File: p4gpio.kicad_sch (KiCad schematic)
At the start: 4 parts, among them J1 C2760486, J2 C2760486

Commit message: Start work on layout
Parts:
- added J10, J9: Conn_01x04_Socket, Connector_PinSocket_2.54mm:PinSocket_1x04_P2.54mm_Vertical, symbol Connector:Conn_01x04_Socket
- added J3, J4, J5, J6, J7, J8: Conn_01x08_Pin, Connector_PinHeader_2.54mm:PinHeader_1x08_P2.54mm_Vertical, symbol Connector:Conn_01x08_Pin
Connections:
- net GND: now also J10.3 (Pin_3), J9.3 (Pin_3)
- net Minimal P4 V3/BOOT renamed BOOT
- net BOOT: now also J10.2 (Pin_2), J9.2 (Pin_2)
- net Minimal P4 V3/CHIP_PU renamed RESET
- net RESET: now also J10.4 (Pin_4), J9.4 (Pin_4)
- new net +3.3V: J10.1 (Pin_1), J9.1 (Pin_1)
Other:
- moved on the sheet: J1, J2

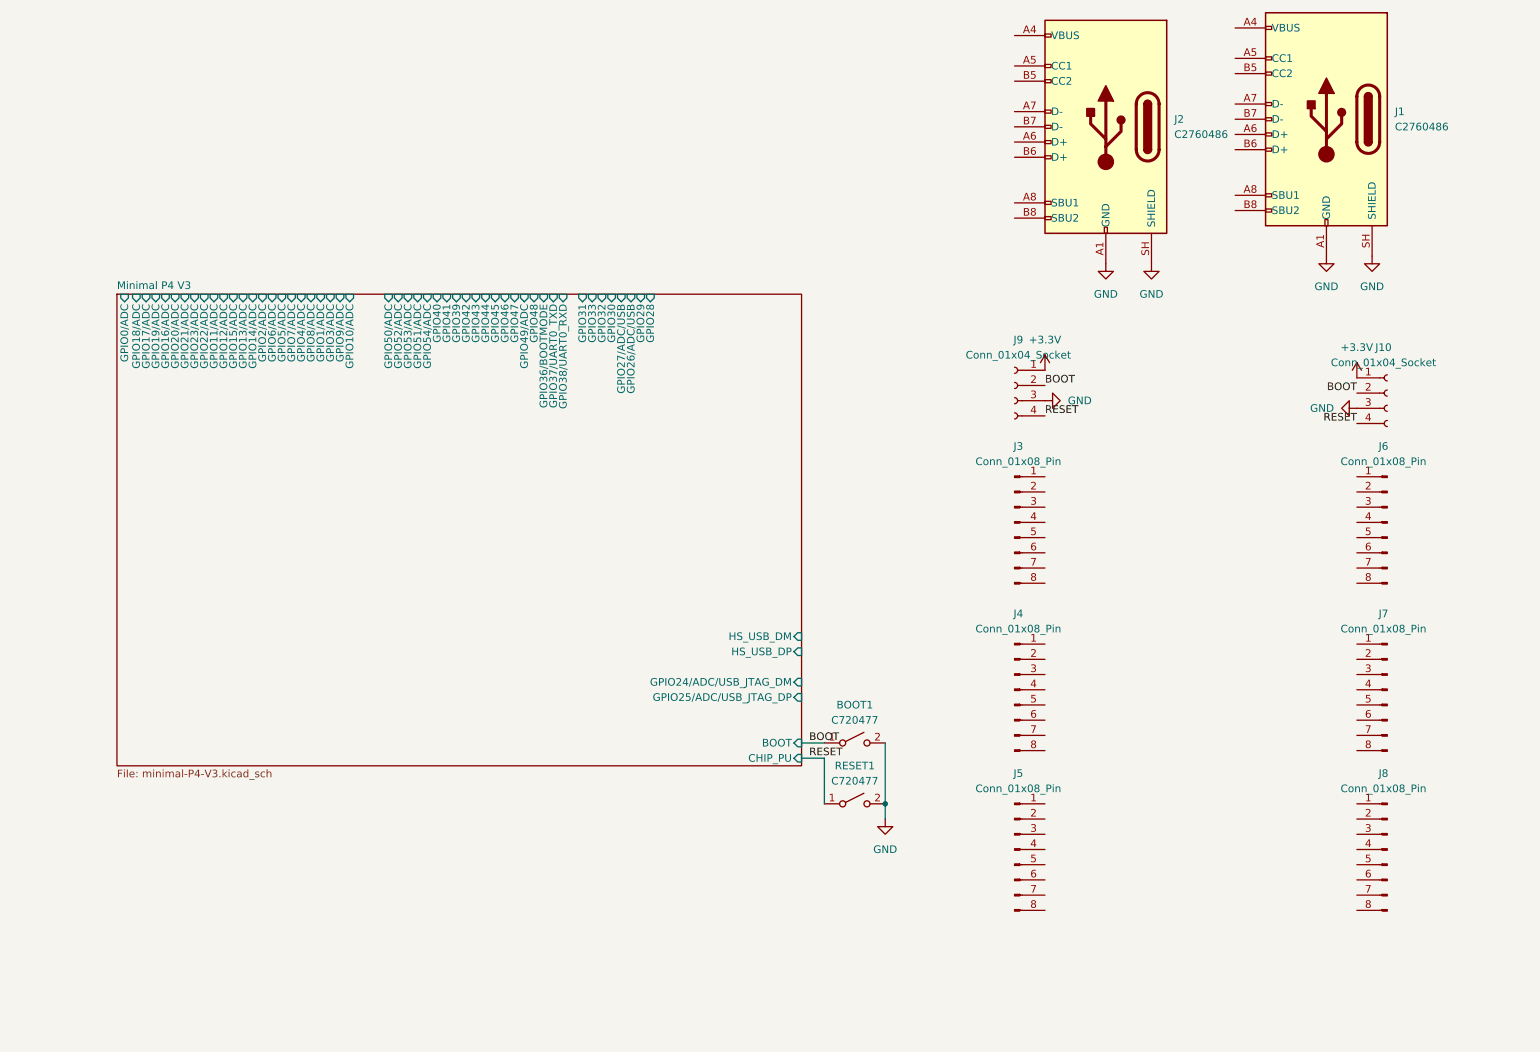
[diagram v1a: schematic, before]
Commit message: Schematic done except for GPIO
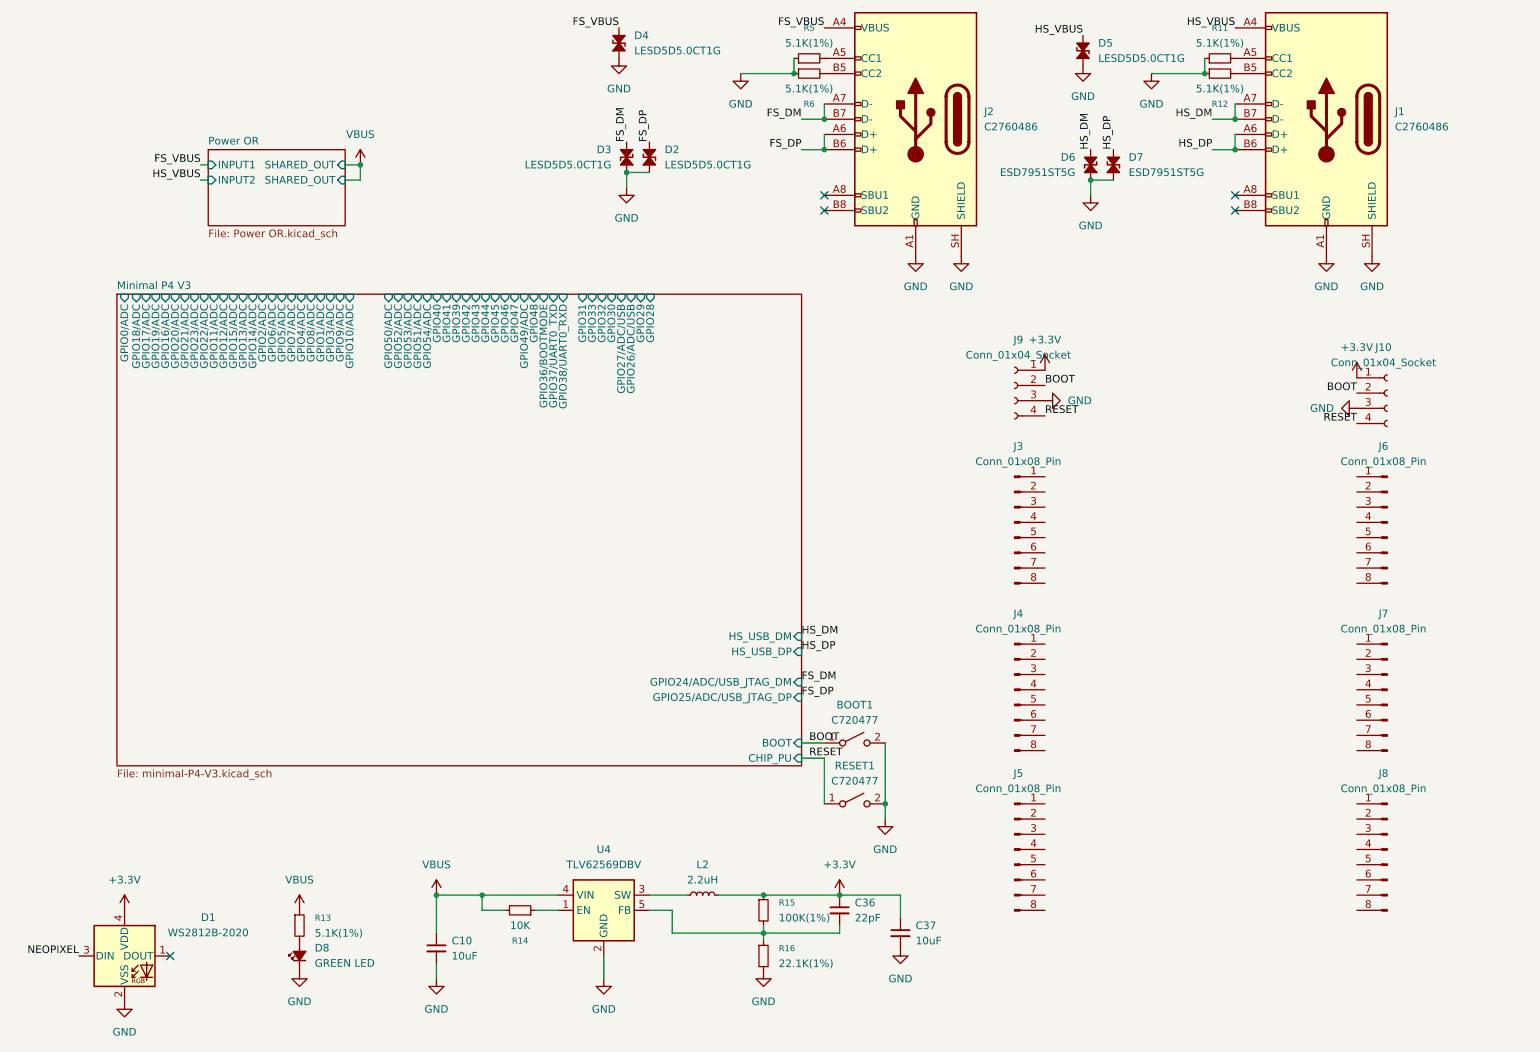
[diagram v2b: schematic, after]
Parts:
- added C10, C37: 10uF, Capacitor_SMD:C_0603_1608Metric, symbol Device:C_Small
- added C36: 22pF, Capacitor_SMD:C_0402_1005Metric, symbol Device:C_Small
- added D1: WS2812B-2020, LED_SMD:LED_WS2812B-2020_PLCC4_2.0x2.0mm, symbol LED:WS2812B-2020
- added D2, D3, D4, D5: LESD5D5.0CT1G, Diode_SMD:D_SOD-523, symbol Device:D_TVS_Small_Filled
- added D6, D7: ESD7951ST5G, Diode_SMD:D_SOD-882, symbol Device:D_TVS_Small_Filled
- added D8: GREEN LED, Diode_SMD:D_0805_2012Metric, symbol Device:LED_Small_Filled
- added L2: 2.2uH, Inductor_SMD:L_1008_2520Metric, symbol Device:L_Small
- added R11, R12, R13, R5, R6: 5.1K(1%), Resistor_SMD:R_0402_1005Metric, symbol Device:R_Small
- added R14: 10K, Resistor_SMD:R_0402_1005Metric, symbol Device:R_Small
- added R15: 100K(1%), Resistor_SMD:R_0402_1005Metric, symbol Device:R_Small
- added R16: 22.1K(1%), Resistor_SMD:R_0402_1005Metric, symbol Device:R_Small
- added U4: TLV62569DBV, Package_TO_SOT_SMD:SOT-23-5, symbol Regulator_Switching:TLV62569DBV
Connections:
- net +3.3V: now also C36.1, C37.1, D1.4 (VDD), L2.2, R15.1
- net GND: now also C10.2, C37.2, D1.2 (VSS), D2.1 (A1), D3.1 (A1), D4.1 (A1), D5.1 (A1), D6.1 (A1), D7.1 (A1), D8.1 (K), R11.1, R12.1, R16.2, R5.1, R6.1, U4.2 (GND)
- net HS_VBUS: now reaches J1.A4 (VBUS), J1.A9 (VBUS), J1.B4 (VBUS), J1.B9 (VBUS)
- net HS_VBUS: now also D5.2 (A2)
- net at J1.A5 (CC1): now also R11.2
- net HS_DP: now reaches J1.A6 (D+)
- net HS_DP: now also J1.B6 (D+), D7.2 (A2)
- net HS_DM: now reaches J1.A7 (D-)
- net HS_DM: now also J1.B7 (D-), D6.2 (A2)
- net at J1.B5 (CC2): now also R12.2
- net FS_VBUS: now reaches J2.A4 (VBUS), J2.A9 (VBUS), J2.B4 (VBUS), J2.B9 (VBUS)
- net FS_VBUS: now also D4.2 (A2)
- net at J2.A5 (CC1): now also R5.2
- net FS_DP: now reaches J2.A6 (D+)
- net FS_DP: now also J2.B6 (D+), D2.2 (A2)
- net FS_DM: now reaches J2.A7 (D-)
- net FS_DM: now also J2.B7 (D-), D3.2 (A2)
- net at J2.B5 (CC2): now also R6.2
- new net: R14.1, U4.1 (EN)
- new net: L2.1, U4.3 (SW)
- new net: C36.2, R15.2, R16.1, U4.5 (FB)
- new net: D8.2 (A), R13.2
- new net NEOPIXEL: D1.3 (DIN)
- new net VBUS: C10.1, R13.1, R14.2, U4.4 (VIN)
- no-connect marks 0 -> 5
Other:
- added sheet Power OR (Power OR.kicad_sch)
- moved on the sheet: J2

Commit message: Setup design rules. Start to match up pins
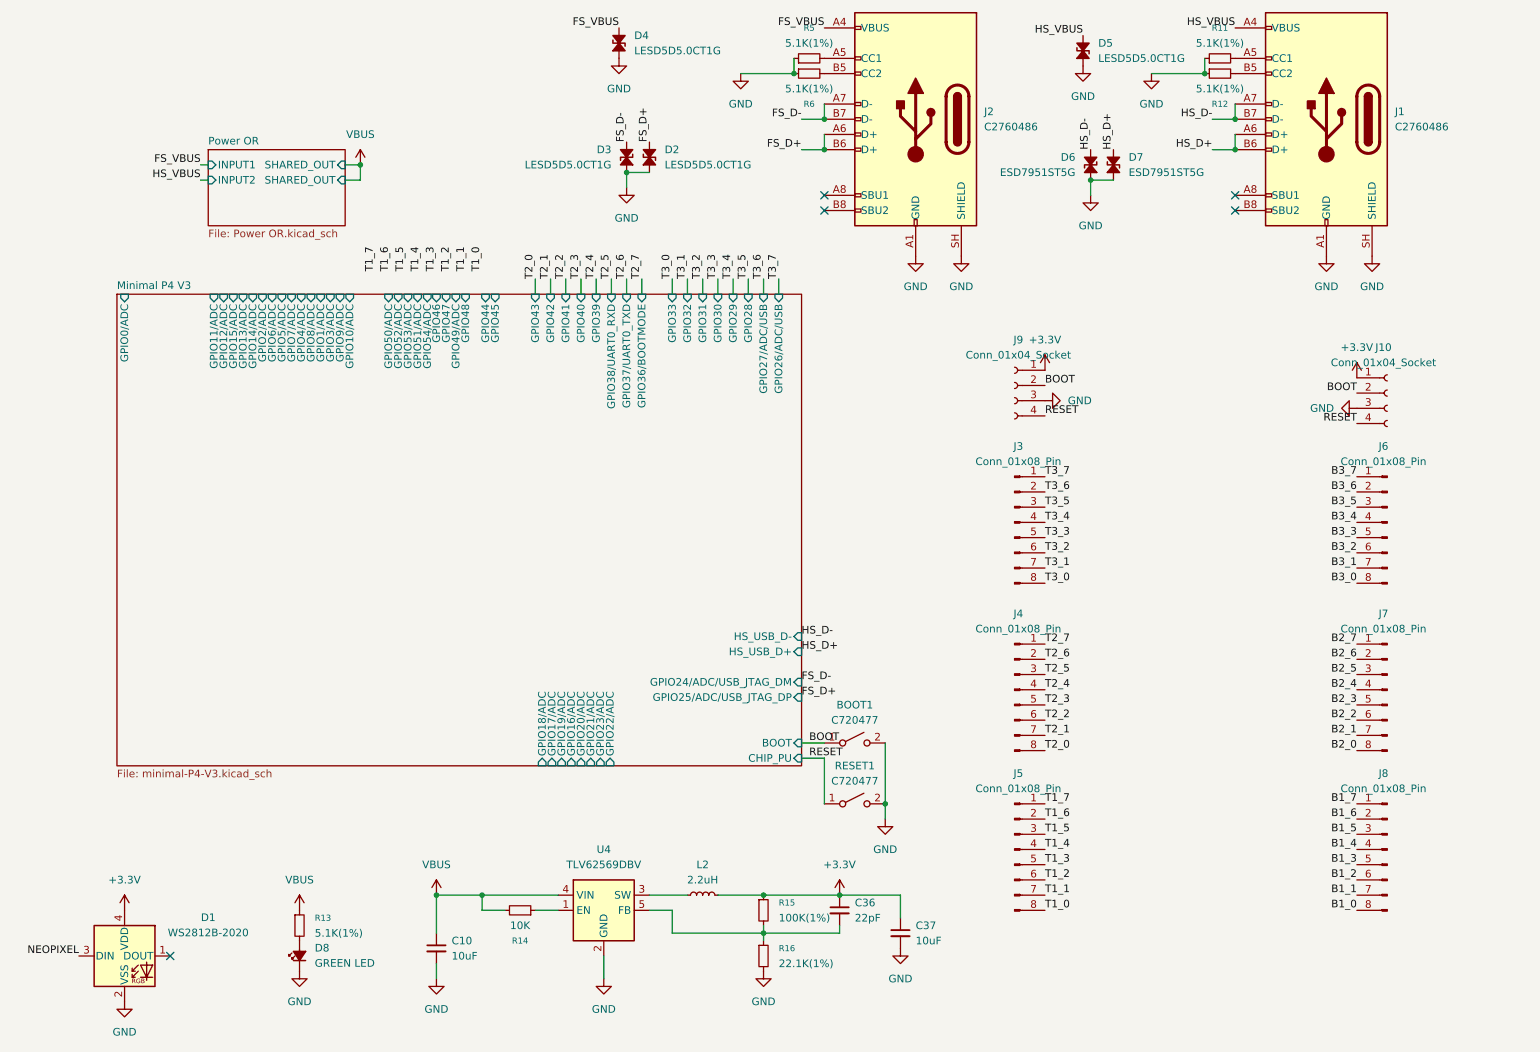
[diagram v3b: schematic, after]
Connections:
- net B3_7: now reaches J6.1 (Pin_1)
- net B3_6: now reaches J6.2 (Pin_2)
- net B3_5: now reaches J6.3 (Pin_3)
- net B3_4: now reaches J6.4 (Pin_4)
- net B3_3: now reaches J6.5 (Pin_5)
- net B3_2: now reaches J6.6 (Pin_6)
- net B3_1: now reaches J6.7 (Pin_7)
- net B3_0: now reaches J6.8 (Pin_8)
- net T2_7: now reaches J4.1 (Pin_1)
- net T2_6: now reaches J4.2 (Pin_2)
- net T2_5: now reaches J4.3 (Pin_3)
- net T2_4: now reaches J4.4 (Pin_4)
- net T2_3: now reaches J4.5 (Pin_5)
- net T2_2: now reaches J4.6 (Pin_6)
- net T2_1: now reaches J4.7 (Pin_7)
- net T2_0: now reaches J4.8 (Pin_8)
- net T3_7: now reaches J3.1 (Pin_1)
- net T3_6: now reaches J3.2 (Pin_2)
- net T3_5: now reaches J3.3 (Pin_3)
- net T3_4: now reaches J3.4 (Pin_4)
- net T3_3: now reaches J3.5 (Pin_5)
- net T3_2: now reaches J3.6 (Pin_6)
- net T3_1: now reaches J3.7 (Pin_7)
- net T3_0: now reaches J3.8 (Pin_8)
- net B2_7: now reaches J7.1 (Pin_1)
- net B2_6: now reaches J7.2 (Pin_2)
- net B2_5: now reaches J7.3 (Pin_3)
- net B2_4: now reaches J7.4 (Pin_4)
- net B2_3: now reaches J7.5 (Pin_5)
- net B2_2: now reaches J7.6 (Pin_6)
- net B2_1: now reaches J7.7 (Pin_7)
- net B2_0: now reaches J7.8 (Pin_8)
- net T1_7: now reaches J5.1 (Pin_1)
- net T1_6: now reaches J5.2 (Pin_2)
- net T1_5: now reaches J5.3 (Pin_3)
- net T1_4: now reaches J5.4 (Pin_4)
- net T1_3: now reaches J5.5 (Pin_5)
- net T1_2: now reaches J5.6 (Pin_6)
- net T1_1: now reaches J5.7 (Pin_7)
- net T1_0: now reaches J5.8 (Pin_8)
- net B1_7: now reaches J8.1 (Pin_1)
- net B1_6: now reaches J8.2 (Pin_2)
- net B1_5: now reaches J8.3 (Pin_3)
- net B1_4: now reaches J8.4 (Pin_4)
- net B1_3: now reaches J8.5 (Pin_5)
- net B1_2: now reaches J8.6 (Pin_6)
- net B1_1: now reaches J8.7 (Pin_7)
- net B1_0: now reaches J8.8 (Pin_8)
- net FS_DM renamed FS_D-
- net FS_DP renamed FS_D+
- net HS_DM renamed HS_D-
- net HS_DP renamed HS_D+
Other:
- sheet Minimal P4 V3 ports: added HS_USB_D+, HS_USB_D-; removed HS_USB_DM, HS_USB_DP

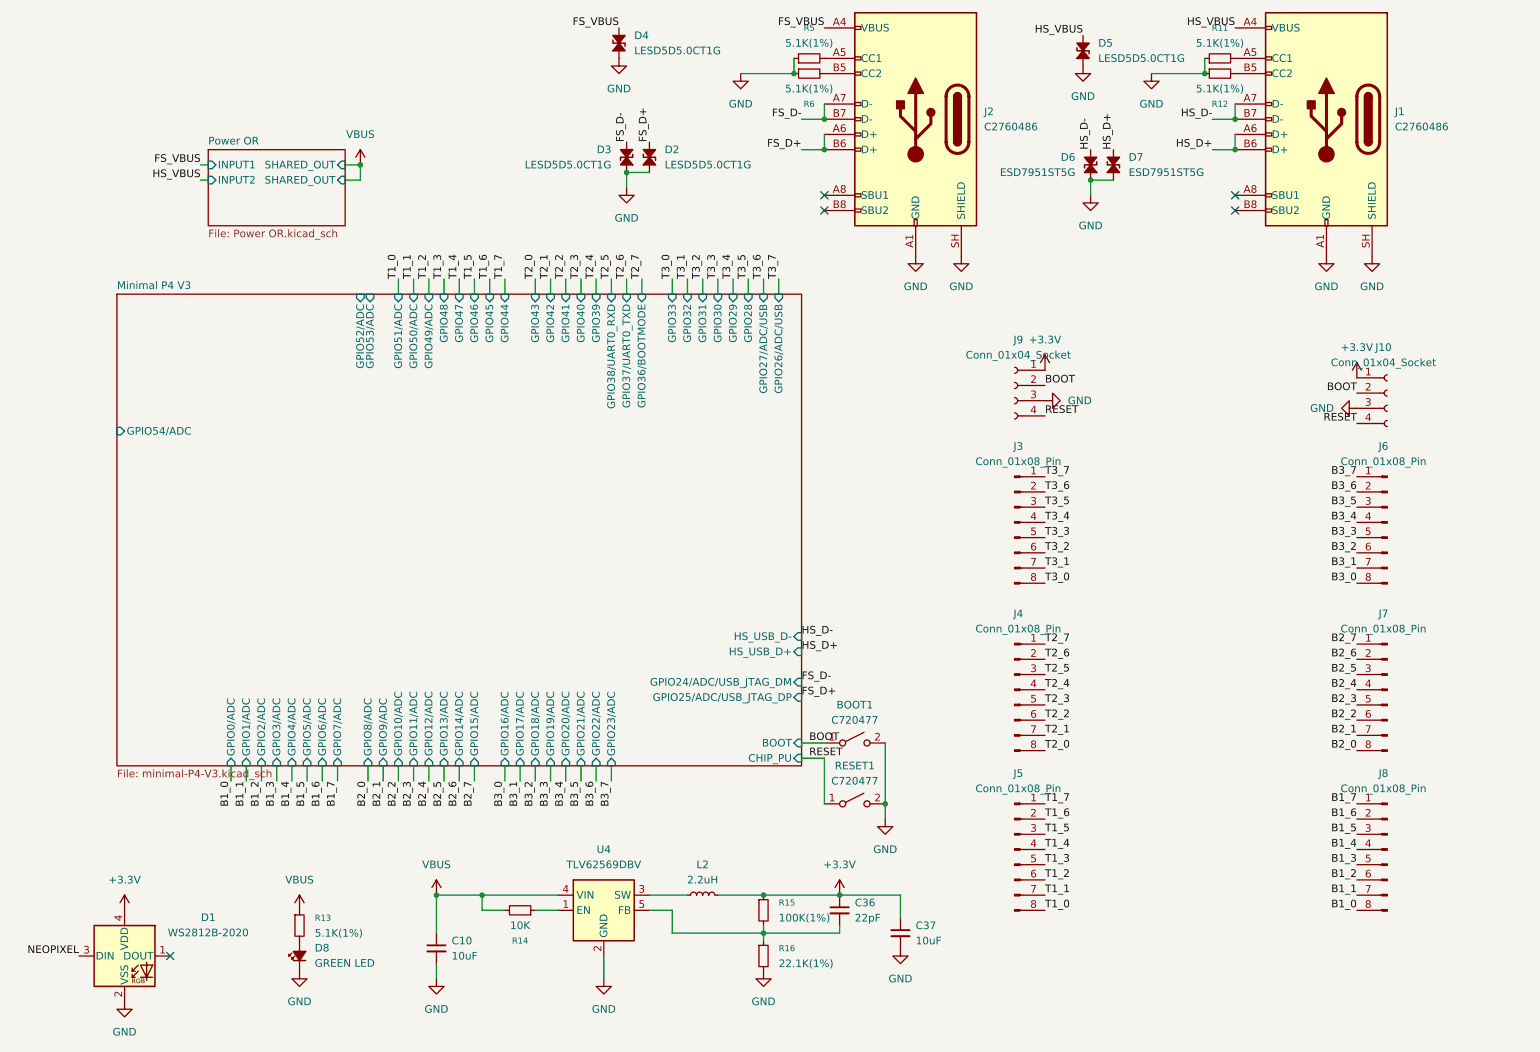
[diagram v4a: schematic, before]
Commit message: Fix bootstrapping pins. Start fixing DRC
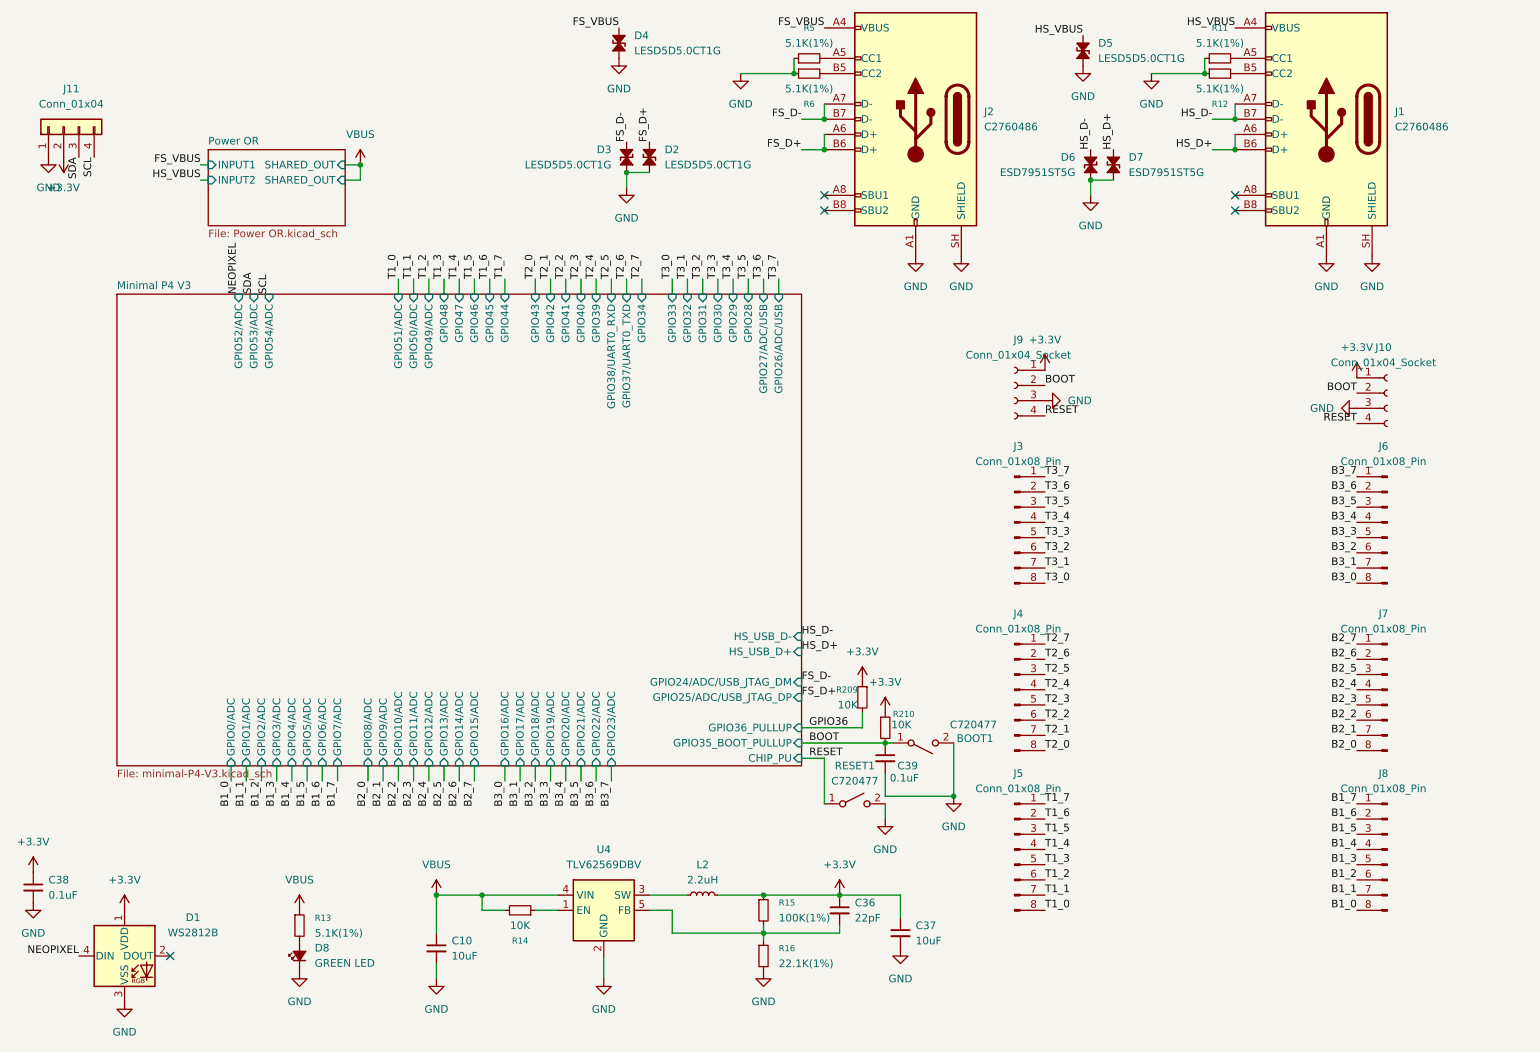
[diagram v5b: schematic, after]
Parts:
- removed D1: WS2812B-2020, LED_SMD:LED_WS2812B-2020_PLCC4_2.0x2.0mm, symbol LED:WS2812B-2020
- added C38, C39: 0.1uF, Capacitor_SMD:C_0402_1005Metric, symbol Device:C_Small
- added D1: WS2812B, LED_SMD:LED_WS2812B_PLCC4_5.0x5.0mm_P3.2mm, symbol LED:WS2812B
- added J11: Conn_01x04, Connector_JST:JST_SH_SM04B-SRSS-TB_1x04-1MP_P1.00mm_Horizontal, symbol Connector_Generic:Conn_01x04
- added R209, R210: 10K, Resistor_SMD:R_0402_1005Metric, symbol Device:R_Small
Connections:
- net +3.3V: now also C38.1, D1.1 (VDD), J11.2 (Pin_2), R209.1, R210.1
- net BOOT: now also C39.1, R210.2
- net GND: now also C38.2, C39.2, D1.3 (VSS), J11.1 (Pin_1)
- net NEOPIXEL: now also D1.4 (DIN)
- new net GPIO36: R209.2
- new net SCL: J11.4 (Pin_4)
- new net SDA: J11.3 (Pin_3)
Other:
- sheet Minimal P4 V3 ports: added GPIO34, GPIO35_BOOT_PULLUP, GPIO36_PULLUP; removed BOOT, GPIO36/BOOTMODE
- moved on the sheet: BOOT1
